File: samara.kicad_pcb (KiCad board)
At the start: 2 copper layers, 239.5 x 118.5 mm, 110 parts, among them J1 AudioJack4, J2 SWD, J3 USB_C_Receptacle_USB2.0, SW1 Boot, U1 W25Q128JVS, U2 RP2040, U3 PRTR5V0U2X, U4 XC6206PxxxMR, Y1 12MHz

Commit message: final, working
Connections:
- L_U2 pad 54: L_SD1 -> L_SD2
- L_U2 pad 55: L_SD2 -> L_SD1
- U2 pad 54: SD1 -> SD2
- U2 pad 55: SD2 -> SD1
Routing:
- net SD1: track 16.1 -> 22.1 mm
- net L_SD1: track 15.4 -> 20.7 mm
- net SD2: track 15.8 -> 19.7 mm
- net L_SD2: track 15.1 -> 18.5 mm
- net CS: track 35.9 -> 37.7 mm
- net L_CS: track 45.5 -> 46.5 mm
- net GND: track 67.1 -> 66.3 mm
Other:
- board size 239.5 x 118.5 mm -> 234.5 x 117.9 mm

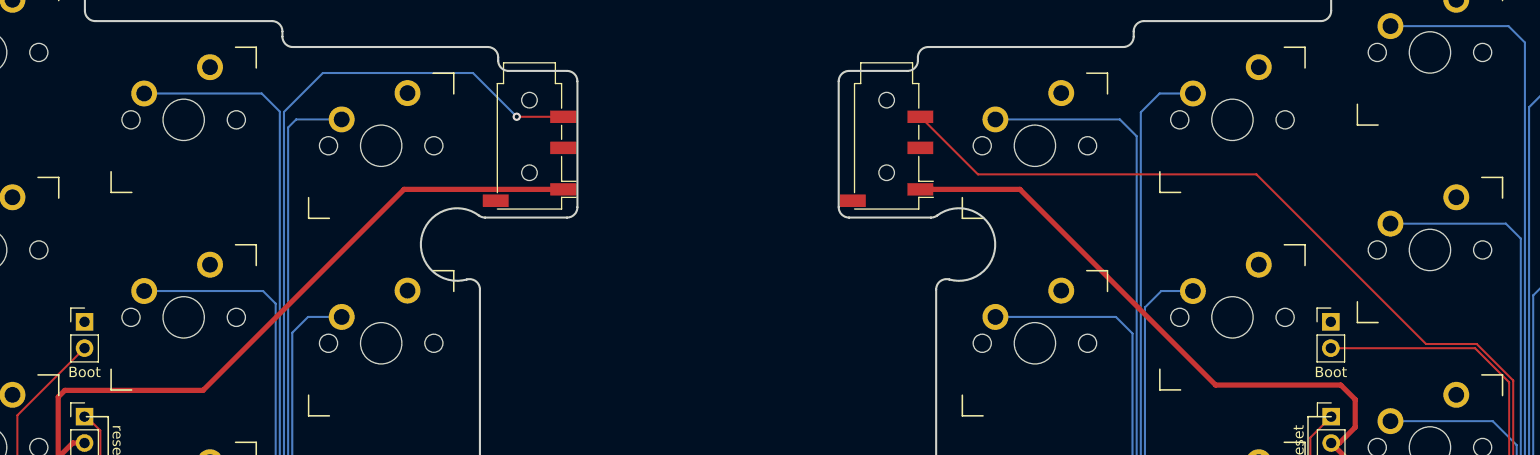
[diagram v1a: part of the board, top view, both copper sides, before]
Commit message: replace trrs
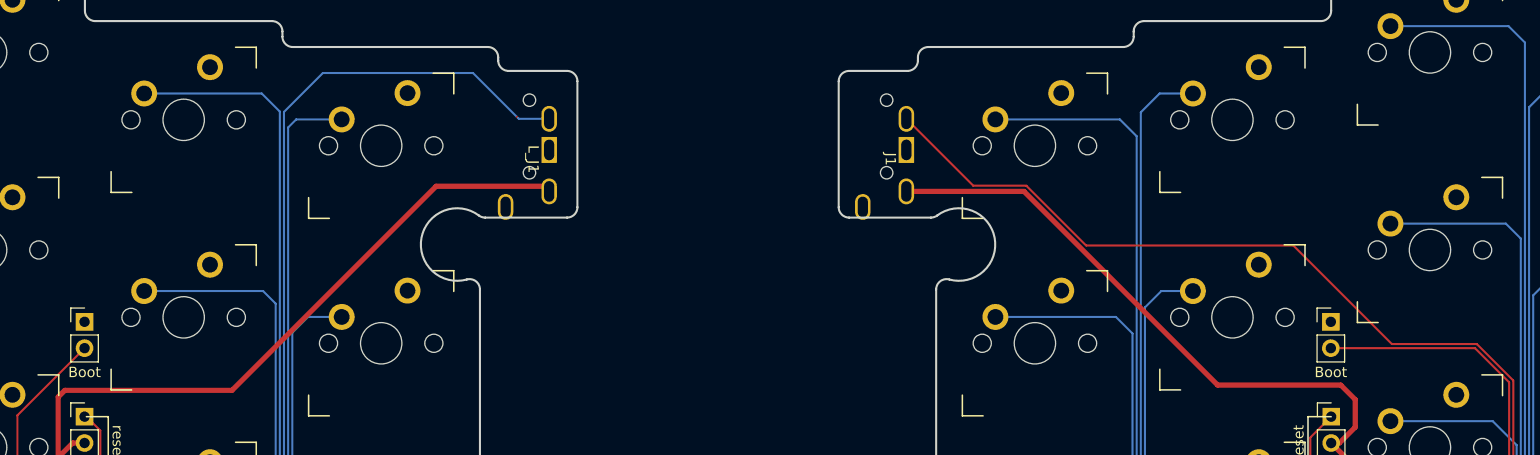
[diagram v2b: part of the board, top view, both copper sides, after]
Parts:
- J1, L_J1: footprint Connector_Audio:Jack_3.5mm_PJ320D_Horizontal -> parts:TRRS-PJ320A
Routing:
- net SERIAL: track 102.6 -> 103.8 mm
- net L_SERIAL: track 131.9 -> 130.6 mm, vias 2 -> 1
